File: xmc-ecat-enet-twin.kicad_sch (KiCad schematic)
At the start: 1 part

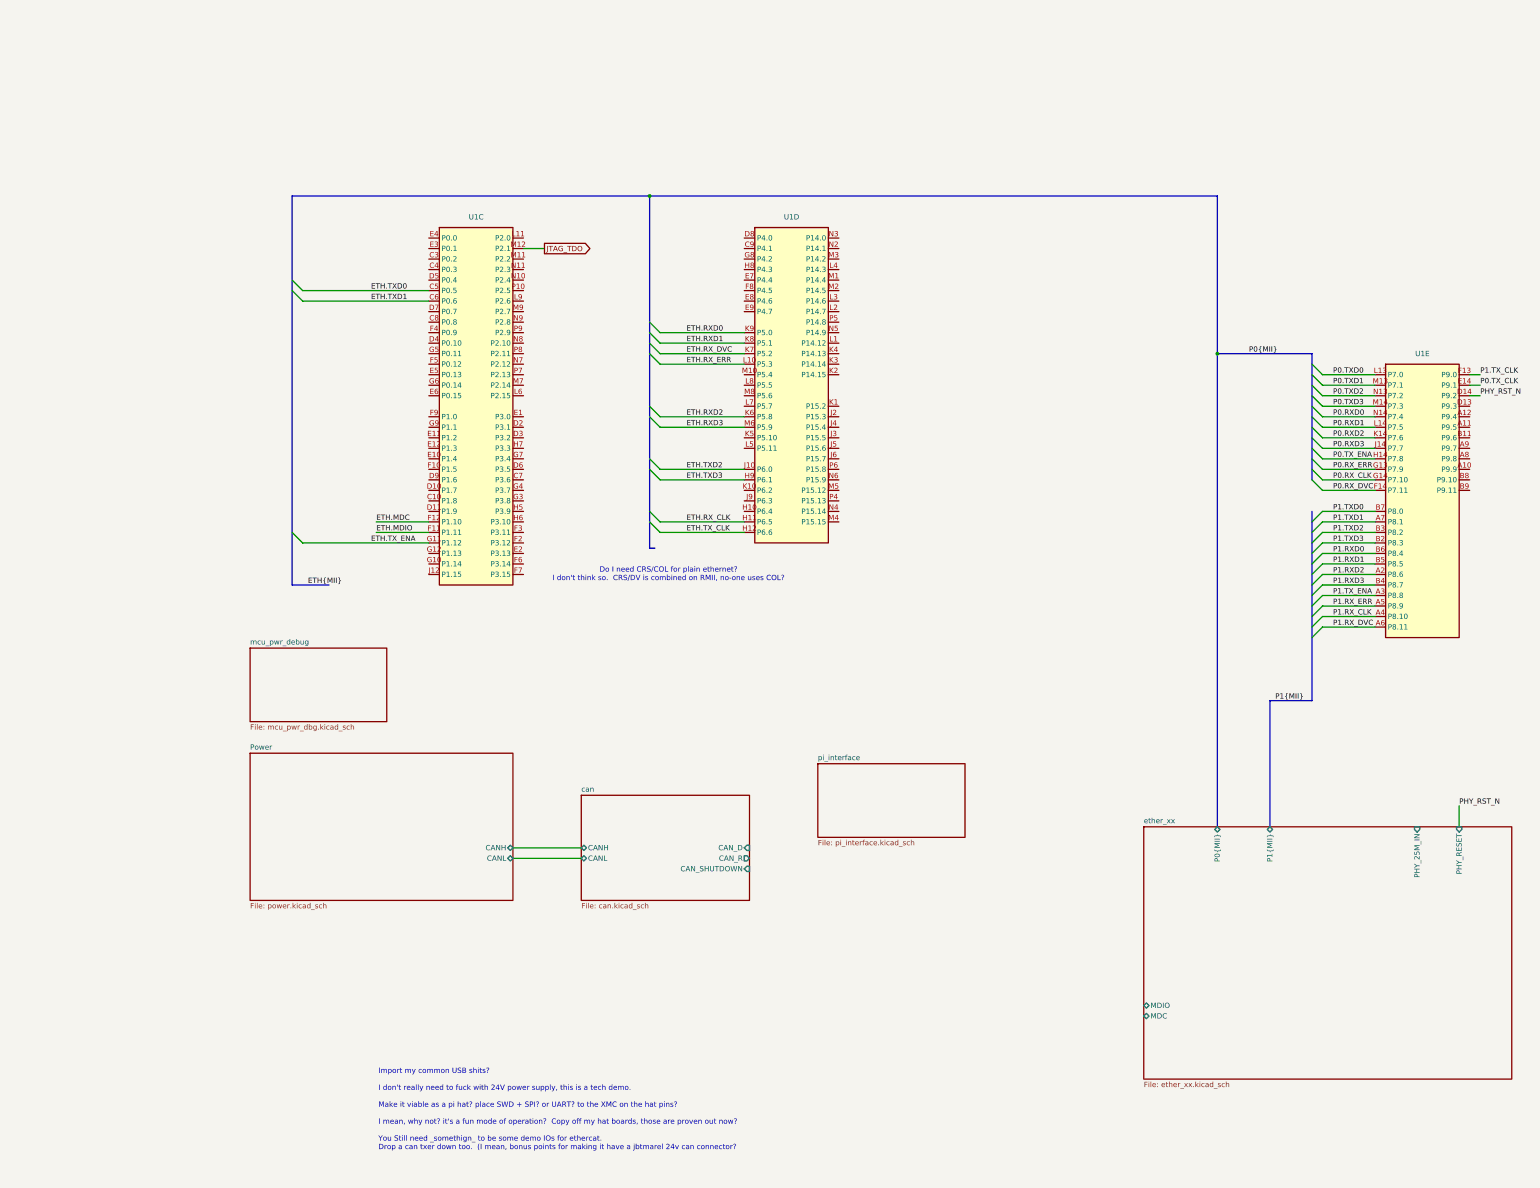
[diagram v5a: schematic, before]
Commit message: push forwards: clock muxing, filling in blanks
Finished off the ethernet section finally.
Sorted a solution to the 25M phy clocks required for ethercat
Connected CAN as per existing hardware (and fixed a bug in speed mode)
Sorted out bypassing for MCU
Added more thoughts on the external interfaces
Started on a 24V supply
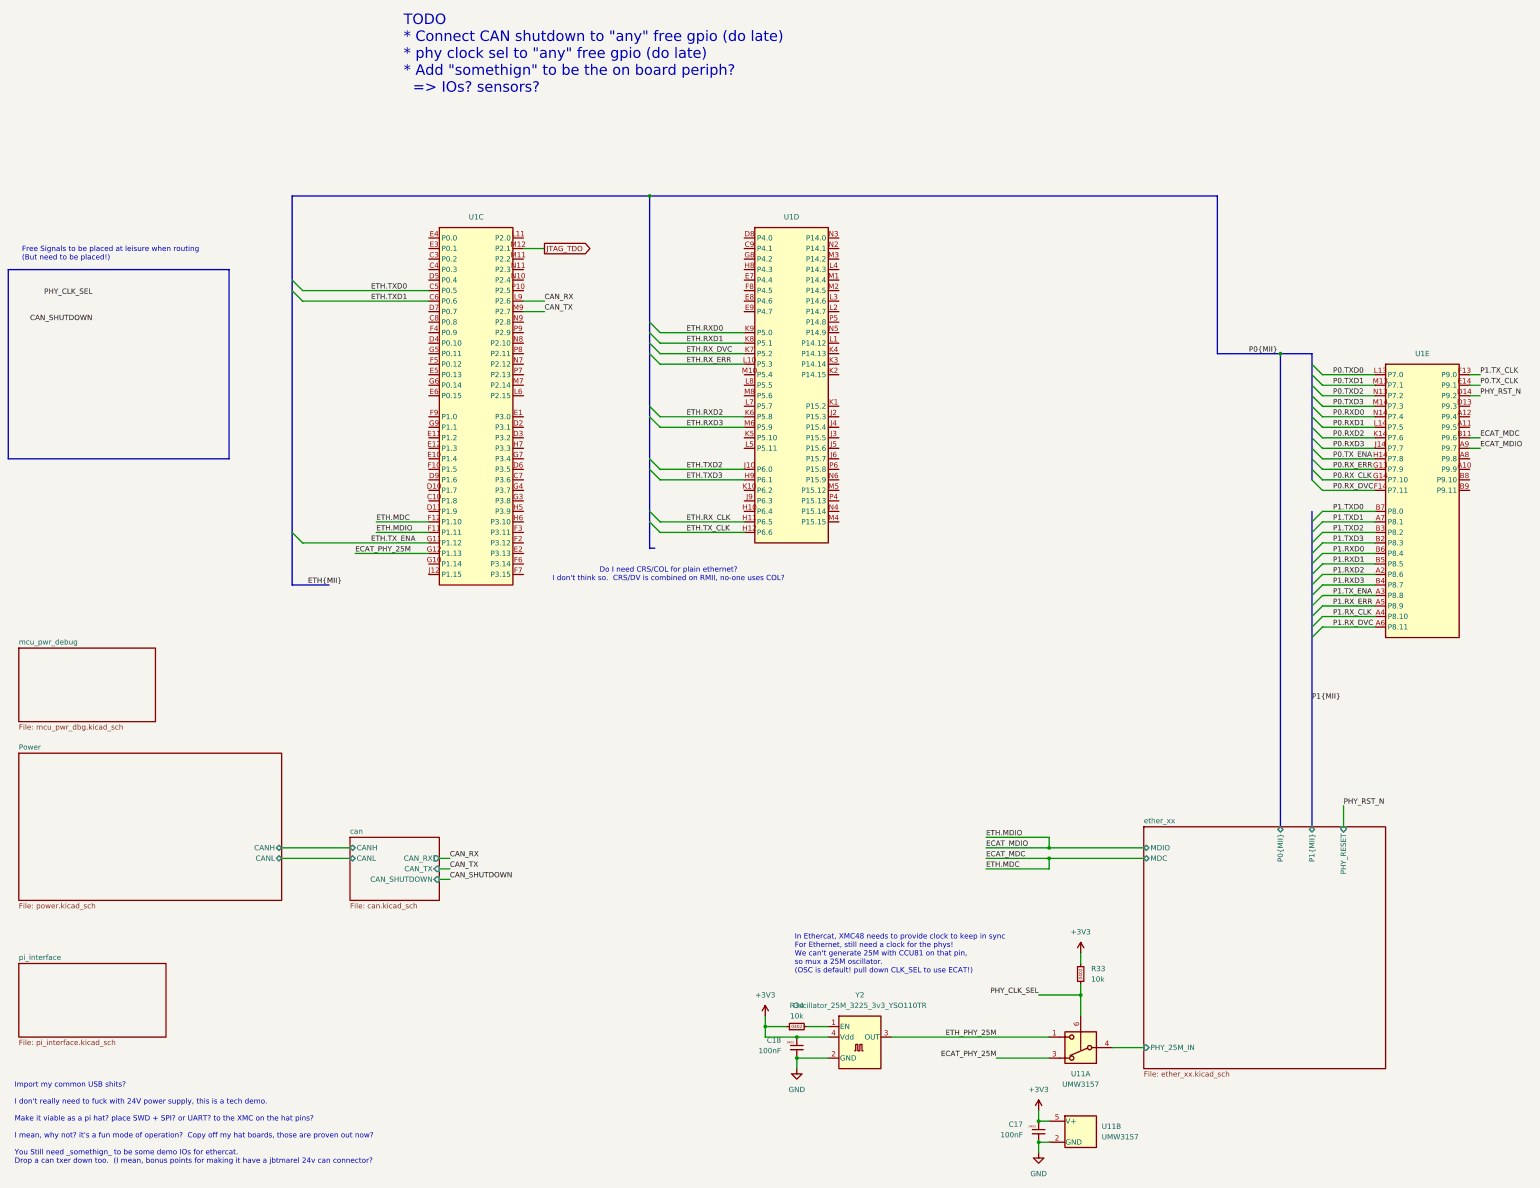
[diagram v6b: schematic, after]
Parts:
- added C17, C18: 100nF, Capacitor_SMD:C_0402_1005Metric, symbol karl-atomic-basic:KC0402_100nF
- added R33, R34: 10k, Resistor_SMD:R_0402_1005Metric, symbol karl-atomic-basic:KR0402_10k
- added U11: UMW3157, Package_TO_SOT_SMD:SOT-363_SC-70-6, symbol karl-parts:Analog_Switch_UMW3157
- added Y2: Oscillator_25M_3225_3v3_YSO110TR, jlc-extras:Oscillator_SMD_3225_YXC_YSO110TR-4Pin_3.2x2.5mm, symbol karl-parts:Oscillator_25M_3225_3v3_YSO110TR
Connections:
- net ETH.MDC is gone; now on net ECAT_MDC: U1.F12 (P1.10)
- net ETH.MDIO is gone; now on net ECAT_MDIO: U1.F11 (P1.11)
- net ether_xx/PHY_25M_IN: now also U11.4
- net ECAT_PHY_25M: now reaches U1.G12 (P1.13)
- net ECAT_PHY_25M: now also U11.3
- net CAN_RX: now reaches U1.L9 (P2.6)
- net CAN_TX: now reaches U1.M9 (P2.7)
- net ECAT_MDIO: now reaches U1.A9 (P9.7)
- net ECAT_MDC: now reaches U1.B11 (P9.6)
- new net: R34.2, Y2.1 (EN)
- new net +3V3: C17.1, C18.1, R33.1, R34.1, U11.5 (V+), Y2.4 (Vdd)
- new net ETH_PHY_25M: U11.1, Y2.3 (OUT)
- new net GND: C17.2, C18.2, U11.2 (GND), Y2.2 (GND)
- new net PHY_CLK_SEL: R33.2, U11.6
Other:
- sheet can ports: added CAN_RX, CAN_TX; removed CAN_D, CAN_R
- note added: "Free Signals to be placed at leisure when routing (But need to be placed!)"
- note added: "In Ethercat, XMC48 needs to provide clock to keep in sync For Ethernet, still need a clock for the phys! We can't generate 25M with CCU81 on that pin, so mux a 25M oscillator. (OSC is default! pull down CLK_SEL to use ECAT!)"
- note added: "TODO * Connect CAN shutdown to "any" free gpio (do late) * phy clock sel to "any" free gpio (do late) * Add "somethign" to be the on board periph? => IOs? sensors?"

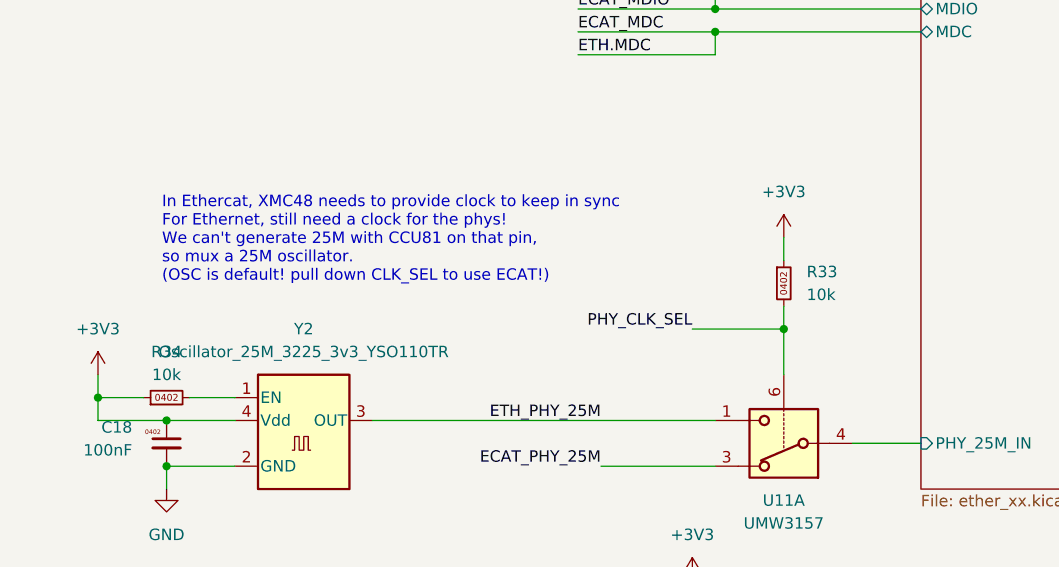
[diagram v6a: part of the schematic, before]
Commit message: sch: make phy clock default to ethercat
This makes it possible to run unmodified 816 fw on this.  (in theory)
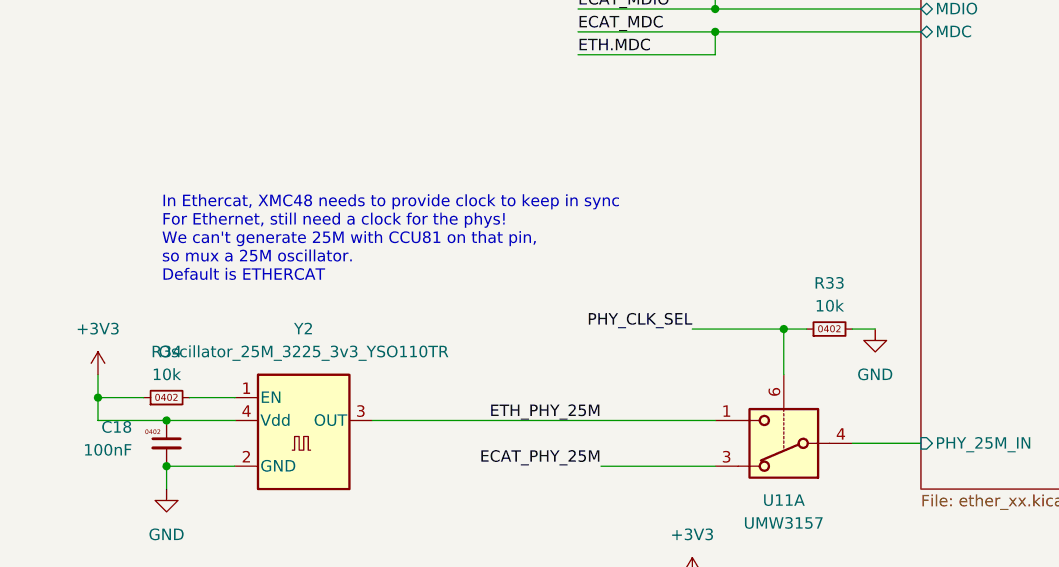
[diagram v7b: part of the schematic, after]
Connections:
- net +3V3: no longer R33.1
- net GND: now also R33.2
- net PHY_CLK_SEL: now also R33.1; no longer R33.2
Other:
- note added: "In Ethercat, XMC48 needs to provide clock to keep in sync For Ethernet, still need a clock for the phys! We can't generate 25M with CCU81 on that pin, so mux a 25M oscillator. Default is ETHERCAT"
- note removed: "In Ethercat, XMC48 needs to provide clock to keep in sync For Ethernet, still need a clock for the phys! We can't generate 25M with CCU81 on that pin, so mux a 25M oscillator. (OSC is default! pull down CLK_SEL to use ECAT!)"
- moved on the sheet: R33
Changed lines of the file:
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@@
 		)
 	)
-	(text "In Ethercat, XMC48 needs to provide clock to keep in sync\nFor Ethernet, still need a clock for the phys!\nWe can't generate 25M with CCU81 on that pin,\nso mux a 25M oscillator.\n(OSC is default! pull down CLK_SEL to use ECAT!)"
+	(text "In Ethercat, XMC48 needs to provide clock to keep in sync\nFor Ethernet, still need a clock for the phys!\nWe can't generate 25M with CCU81 on that pin,\nso mux a 25M oscillator.\nDefault is ETHERCAT"
 		(exclude_from_sim no)
 		(at 212.852 200.914 0)
@@
 	)
 	(junction
+		(at 281.94 210.82)
+		(diameter 0)
+		(color 0 0 0 0)
+	)
+	(junction
 		(at 213.36 220.98)
 		(diameter 0)
@@
 	)
 	(junction
-		(at 281.94 210.82)
-		(diameter 0)
-		(color 0 0 0 0)
-	)
-	(junction
 		(at 271.78 246.38)
 		(diameter 0)
@@
 	(wire
 		(pts
-			(xy 281.94 208.28) (xy 281.94 210.82)
-		)
-		(stroke
-			(width 0)
-			(type default)
-		)
-	)
-	(wire
-		(pts
 			(xy 340.36 86.36) (xy 353.06 86.36)
 		)
@@
 	(wire
 		(pts
+			(xy 284.48 210.82) (xy 281.94 210.82)
+		)
+		(stroke
+			(width 0)
+			(type default)
+		)
+	)
+	(wire
+		(pts
 			(xy 340.36 76.2) (xy 353.06 76.2)
 		)
@@
 	(wire
 		(pts
+			(xy 292.1 210.82) (xy 289.56 210.82)
+		)
+		(stroke
+			(width 0)
+			(type default)
+		)
+	)
+	(wire
+		(pts
 			(xy 340.36 116.84) (xy 353.06 116.84)
 		)
@@
 	(wire
 		(pts
-			(xy 281.94 200.66) (xy 281.94 203.2)
-		)
-		(stroke
-			(width 0)
-			(type default)
-		)
-	)
-	(wire
-		(pts
 			(xy 205.74 218.44) (xy 210.82 218.44)
 		)
@@
 	(symbol
 		(lib_id "karl-atomic-basic:KR0402_10k")
-		(at 281.94 205.74 0)
+		(at 287.02 210.82 90)
 		(unit 1)
 		(body_style 1)
@@
 		(fields_autoplaced yes)
 		(property "Reference" "R33"
-			(at 284.48 204.4699 0)
+			(at 287.02 205.74 90)
 			(show_name no)
 			(do_not_autoplace no)
@@
 					(size 1.27 1.27)
 				)
-				(justify left)
 			)
 		)
 		(property "Value" "10k"
-			(at 284.48 207.0099 0)
+			(at 287.02 208.28 90)
 			(show_name no)
 			(do_not_autoplace no)
@@
 					(size 1.27 1.27)
 				)
-				(justify left)
 			)
 		)
 		(property "Footprint" "Resistor_SMD:R_0402_1005Metric"
-			(at 281.94 205.74 0)
+			(at 287.02 210.82 0)
 			(hide yes)
 			(show_name no)
@@
 		)
 		(property "Datasheet" ""
-			(at 281.94 205.74 0)
+			(at 287.02 210.82 0)
 			(hide yes)
 			(show_name no)
@@
 		)
 		(property "Description" "Resistor, 0402"
-			(at 281.94 205.74 0)
+			(at 287.02 210.82 0)
 			(hide yes)
 			(show_name no)
@@
 		)
 		(property "LCSC Part #" "C25744"
-			(at 281.94 205.74 0)
+			(at 287.02 210.82 0)
 			(hide yes)
 			(show_name no)
@@
 		)
 		(property "MPN" "0402WGF1002TCE"
-			(at 281.94 205.74 0)
+			(at 287.02 210.82 0)
 			(hide yes)
 			(show_name no)
@@
 		)
 		(property "jlcbasic" "basic"
-			(at 281.94 205.74 0)
+			(at 287.02 210.82 0)
 			(hide yes)
 			(show_name no)
@@
 	)
 	(symbol
-		(lib_id "power:+3V3")
-		(at 281.94 200.66 0)
-		(unit 1)
-		(body_style 1)
-		(exclude_from_sim no)
-		(in_bom yes)
-		(on_board yes)
-		(in_pos_files yes)
-		(dnp no)
-		(fields_autoplaced yes)
-		(property "Reference" "#PWR053"
-			(at 281.94 204.47 0)
-			(hide yes)
-			(show_name no)
-			(do_not_autoplace no)
-			(effects
-				(font
-					(size 1.27 1.27)
-				)
-			)
-		)
-		(property "Value" "+3V3"
-			(at 281.94 195.58 0)
-			(show_name no)
-			(do_not_autoplace no)
-			(effects
-				(font
-					(size 1.27 1.27)
-				)
-			)
-		)
-		(property "Footprint" ""
-			(at 281.94 200.66 0)
-			(hide yes)
-			(show_name no)
-			(do_not_autoplace no)
-			(effects
-				(font
-					(size 1.27 1.27)
-				)
-			)
-		)
-		(property "Datasheet" ""
-			(at 281.94 200.66 0)
-			(hide yes)
-			(show_name no)
-			(do_not_autoplace no)
-			(effects
-				(font
-					(size 1.27 1.27)
-				)
-			)
-		)
-		(property "Description" "Power symbol creates a global label with name \"+3V3\""
-			(at 281.94 200.66 0)
-			(hide yes)
-			(show_name no)
-			(do_not_autoplace no)
-			(effects
-				(font
-					(size 1.27 1.27)
-				)
-			)
-		)
-		(pin "1"
-		)
-		(instances
-			(project "xmc-ecat-enet-twin"
-				(path "/f5c7c34d-e330-4aa5-be7e-80f0a3a977af"
-					(reference "#PWR053")
-					(unit 1)
-				)
-			)
-		)
-	)
-	(symbol
 		(lib_id "karl-parts:XMC4800_E196x")
 		(at 127 25.4 0)
@@
 	)
 	(symbol
+		(lib_id "power:GND")
+		(at 292.1 210.82 0)
+		(unit 1)
+		(body_style 1)
+		(exclude_from_sim no)
+		(in_bom yes)
+		(on_board yes)
+		(in_pos_files yes)
+		(dnp no)
+		(fields_autoplaced yes)
+		(property "Reference" "#PWR053"
+			(at 292.1 217.17 0)
+			(hide yes)
+			(show_name no)
+			(do_not_autoplace no)
+			(effects
+				(font
+					(size 1.27 1.27)
+				)
+			)
+		)
+		(property "Value" "GND"
+			(at 292.1 215.9 0)
+			(show_name no)
+			(do_not_autoplace no)
+			(effects
+				(font
+					(size 1.27 1.27)
+				)
+			)
+		)
+		(property "Footprint" ""
+			(at 292.1 210.82 0)
+			(hide yes)
+			(show_name no)
+			(do_not_autoplace no)
+			(effects
+				(font
+					(size 1.27 1.27)
+				)
+			)
+		)
+		(property "Datasheet" ""
+			(at 292.1 210.82 0)
+			(hide yes)
+			(show_name no)
+			(do_not_autoplace no)
+			(effects
+				(font
+					(size 1.27 1.27)
+				)
+			)
+		)
+		(property "Description" "Power symbol creates a global label with name \"GND\" , ground"
+			(at 292.1 210.82 0)
+			(hide yes)
+			(show_name no)
+			(do_not_autoplace no)
+			(effects
+				(font
+					(size 1.27 1.27)
+				)
+			)
+		)
+		(pin "1"
+		)
+		(instances
+			(project "xmc-ecat-enet-twin"
+				(path "/f5c7c34d-e330-4aa5-be7e-80f0a3a977af"
+					(reference "#PWR053")
+					(unit 1)
+				)
+			)
+		)
+	)
+	(symbol
 		(lib_id "karl-parts:Oscillator_25M_3225_3v3_YSO110TR")
 		(at 228.6 223.52 0)
@@
 		(in_pos_files yes)
 		(dnp no)
-		(fields_autoplaced yes)
 		(property "Reference" "U11"
 			(at 281.94 229.87 0)
